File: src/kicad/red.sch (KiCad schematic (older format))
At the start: 0 parts

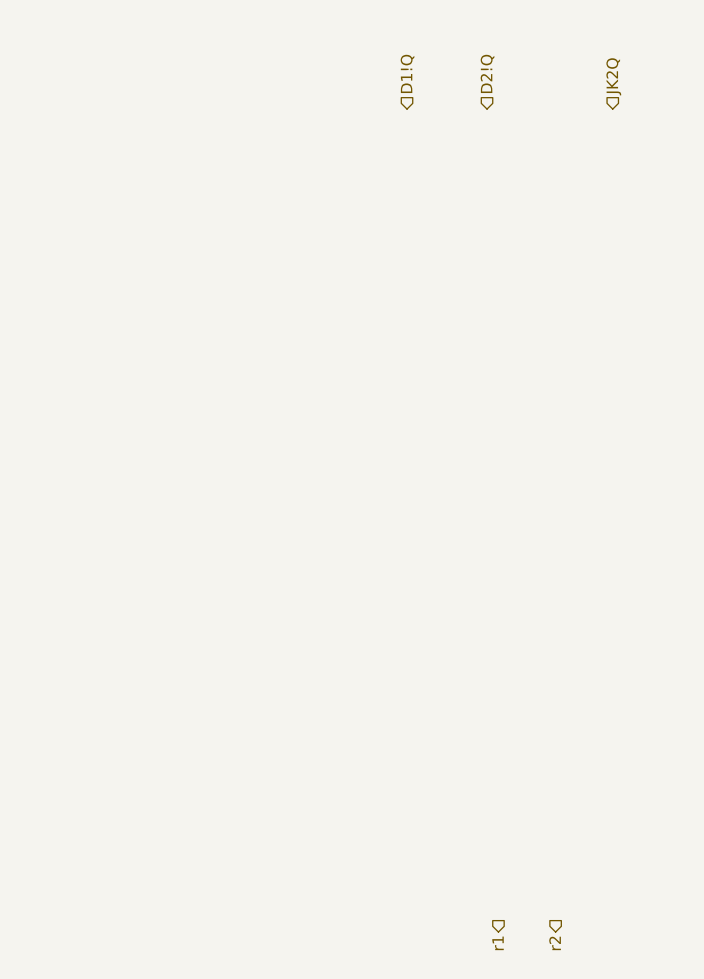
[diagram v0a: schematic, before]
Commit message: finished sub-schemes for LEDs
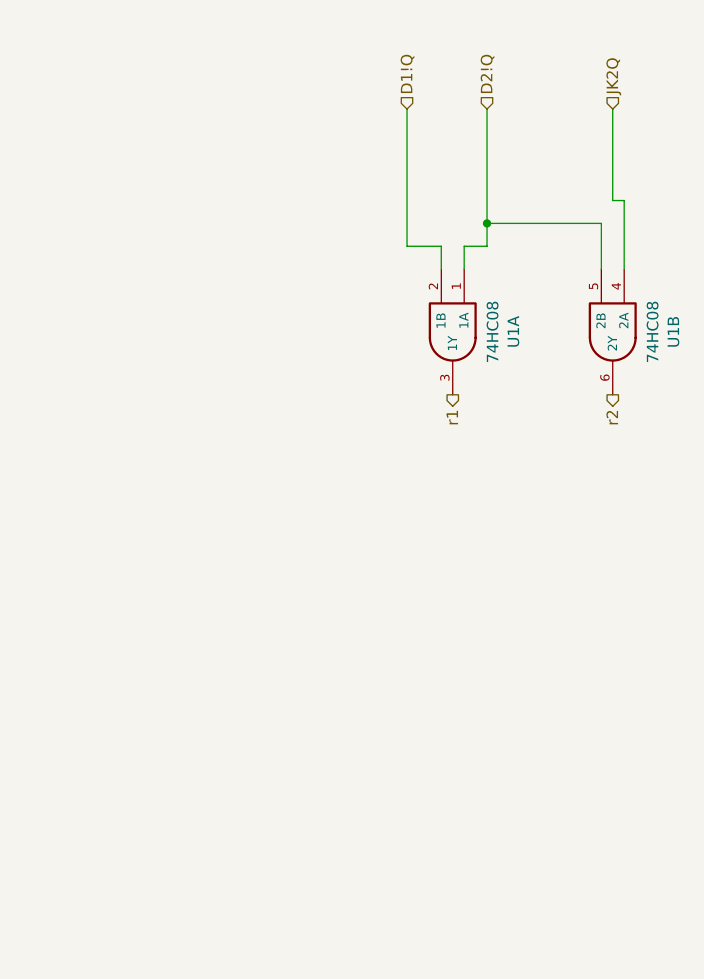
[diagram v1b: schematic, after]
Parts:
- added U1: 74HC08, Housings_SOIC:SOIC-14_3.9x8.7mm_Pitch1.27mm, symbol PB170:74HC08
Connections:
- net D1!Q: now also U1.2 (1B)
- net D2!Q: now also U1.1 (1A), U1.5 (2B)
- net JK2Q: now also U1.4 (2A)
- net r1: now also U1.3 (1Y)
- net r2: now also U1.6 (2Y)
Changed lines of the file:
@@
 Text HLabel 3650 2300 1    50   Input ~ 0
 JK2Q
-Text HLabel 3150 5850 3    50   Output ~ 0
+Text HLabel 2950 3550 3    50   Output ~ 0
 r1
-Text HLabel 3400 5850 3    50   Output ~ 0
+Text HLabel 3650 3550 3    50   Output ~ 0
 r2
+$Comp
+L PB170:74HC08 U?
+U 1 1 5FFDC9CB
+P 2950 3250
+AR Path="/5FFDC9CB" Ref="U?"  Part="2"
+AR Path="/6009AD55/5FFDC9CB" Ref="U1"  Part="1"
+F 0 "U1" H 2975 3517 50  0000 C CNN
+F 1 "74HC08" H 2975 3426 50  0000 C CNN
+F 2 "Housings_SOIC:SOIC-14_3.9x8.7mm_Pitch1.27mm" H 2950 3250 50  0001 C CNN
+F 3 "https://datasheet.lcsc.com/szlcsc/Nexperia-74HC08D-653_C5593.pdf" H 2950 3250 50  0001 C CNN
+F 4 "C5593" H 2950 3250 50  0001 C CNN "LCSC"
+	1    2950 3250
+	0    1    1    0
+$EndComp
+$Comp
+L PB170:74HC08 U?
+U 2 1 5FFDE494
+P 3650 3250
+AR Path="/5FFDE494" Ref="U?"  Part="2"
+AR Path="/6009AD55/5FFDE494" Ref="U1"  Part="2"
+F 0 "U1" H 3675 3517 50  0000 C CNN
+F 1 "74HC08" H 3675 3426 50  0000 C CNN
+F 2 "Housings_SOIC:SOIC-14_3.9x8.7mm_Pitch1.27mm" H 3650 3250 50  0001 C CNN
+F 3 "https://datasheet.lcsc.com/szlcsc/Nexperia-74HC08D-653_C5593.pdf" H 3650 3250 50  0001 C CNN
+F 4 "C5593" H 3650 3250 50  0001 C CNN "LCSC"
+	2    3650 3250
+	0    1    1    0
+$EndComp
+Wire Wire Line
+	2750 2300 2750 2900
+Wire Wire Line
+	2750 2900 2900 2900
+Wire Wire Line
+	2900 2900 2900 3000
+Wire Wire Line
+	3100 2300 3100 2800
+Wire Wire Line
+	3100 2900 3000 2900
+Wire Wire Line
+	3000 2900 3000 3000
+Wire Wire Line
+	3650 2300 3650 2700
+Wire Wire Line
+	3650 2700 3700 2700
+Wire Wire Line
+	3700 2700 3700 3000
+Wire Wire Line
+	3100 2800 3600 2800
+Wire Wire Line
+	3600 2800 3600 3000
+Connection ~ 3100 2800
+Wire Wire Line
+	3100 2800 3100 2900
 $EndSCHEMATC

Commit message: Partially fixed footprint library and reassigning references
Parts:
- U1: footprint Housings_SOIC:SOIC-14_3.9x8.7mm_Pitch1.27mm -> Housing_SOIC:SOIC-14_3.9x8.7mm_Pitch1.27mm
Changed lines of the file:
@@
 F 0 "U1" H 3675 3517 50  0000 C CNN
 F 1 "74HC08" H 3675 3426 50  0000 C CNN
-F 2 "Housings_SOIC:SOIC-14_3.9x8.7mm_Pitch1.27mm" H 3650 3250 50  0001 C CNN
+F 2 "Housing_SOIC:SOIC-14_3.9x8.7mm_Pitch1.27mm" H 3650 3250 50  0001 C CNN
 F 3 "https://datasheet.lcsc.com/szlcsc/Nexperia-74HC08D-653_C5593.pdf" H 3650 3250 50  0001 C CNN
 F 4 "C5593" H 3650 3250 50  0001 C CNN "LCSC"
@@
 F 0 "U1" H 2975 3517 50  0000 C CNN
 F 1 "74HC08" H 2975 3426 50  0000 C CNN
-F 2 "Housings_SOIC:SOIC-14_3.9x8.7mm_Pitch1.27mm" H 2950 3250 50  0001 C CNN
+F 2 "Housing_SOIC:SOIC-14_3.9x8.7mm_Pitch1.27mm" H 2950 3250 50  0001 C CNN
 F 3 "https://datasheet.lcsc.com/szlcsc/Nexperia-74HC08D-653_C5593.pdf" H 2950 3250 50  0001 C CNN
 F 4 "C5593" H 2950 3250 50  0001 C CNN "LCSC"

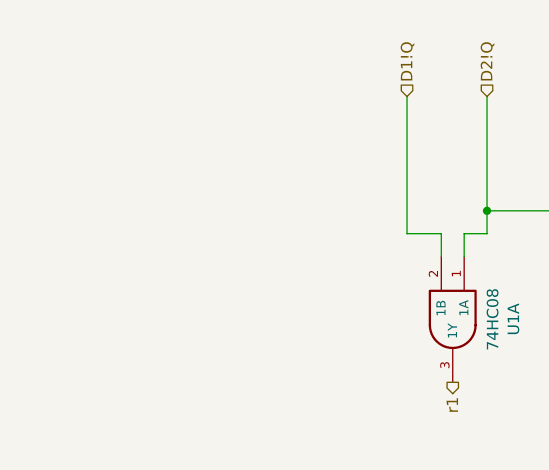
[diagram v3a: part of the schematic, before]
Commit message: added annotations, power connections to parts
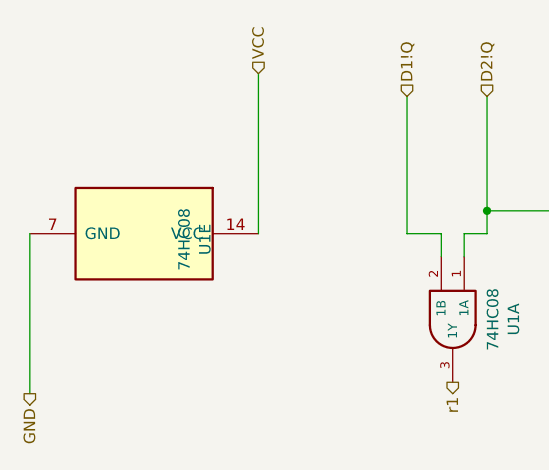
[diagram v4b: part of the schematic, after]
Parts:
- added unit 5 of U1
- U1: footprint Housing_SOIC:SOIC-14_3.9x8.7mm_Pitch1.27mm -> Package_SO:SOIC-14_3.9x8.7mm_P1.27mm
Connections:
- new net GND: U1.7 (GND)
- new net VCC: U1.14 (VCC)
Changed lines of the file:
@@
 F 0 "U1" H 3675 3517 50  0000 C CNN
 F 1 "74HC08" H 3675 3426 50  0000 C CNN
-F 2 "Housing_SOIC:SOIC-14_3.9x8.7mm_Pitch1.27mm" H 3650 3250 50  0001 C CNN
+F 2 "Package_SO:SOIC-14_3.9x8.7mm_P1.27mm" H 3650 3250 50  0001 C CNN
 F 3 "https://datasheet.lcsc.com/szlcsc/Nexperia-74HC08D-653_C5593.pdf" H 3650 3250 50  0001 C CNN
 F 4 "C5593" H 3650 3250 50  0001 C CNN "LCSC"
@@
 F 0 "U1" H 2975 3517 50  0000 C CNN
 F 1 "74HC08" H 2975 3426 50  0000 C CNN
-F 2 "Housing_SOIC:SOIC-14_3.9x8.7mm_Pitch1.27mm" H 2950 3250 50  0001 C CNN
+F 2 "Package_SO:SOIC-14_3.9x8.7mm_P1.27mm" H 2950 3250 50  0001 C CNN
 F 3 "https://datasheet.lcsc.com/szlcsc/Nexperia-74HC08D-653_C5593.pdf" H 2950 3250 50  0001 C CNN
 F 4 "C5593" H 2950 3250 50  0001 C CNN "LCSC"
@@
 	0    1    1    0
 $EndComp
+$Comp
+L PB170:74HC08 U?
+U 5 1 606E2846
+P 1600 2900
+AR Path="/606E2846" Ref="U?"  Part="2"
+AR Path="/6006FC3B/606E2846" Ref="U?"  Part="4"
+AR Path="/6004480C/606E2846" Ref="U?"  Part="5"
+AR Path="/6009AD55/606E2846" Ref="U1"  Part="5"
+F 0 "U1" H 1625 3167 50  0000 C CNN
+F 1 "74HC08" H 1625 3076 50  0000 C CNN
+F 2 "Package_SO:SOIC-14_3.9x8.7mm_P1.27mm" H 1600 2900 50  0001 C CNN
+F 3 "https://datasheet.lcsc.com/szlcsc/Nexperia-74HC08D-653_C5593.pdf" H 1600 2900 50  0001 C CNN
+F 4 "C5593" H 1600 2900 50  0001 C CNN "LCSC"
+	5    1600 2900
+	0    1    1    0
+$EndComp
+Wire Wire Line
+	2100 2900 2100 2200
+Wire Wire Line
+	1100 2900 1100 3600
+Text HLabel 2100 2200 1    50   Input ~ 0
+VCC
+Text HLabel 1100 3600 3    50   Output ~ 0
+GND
 $EndSCHEMATC

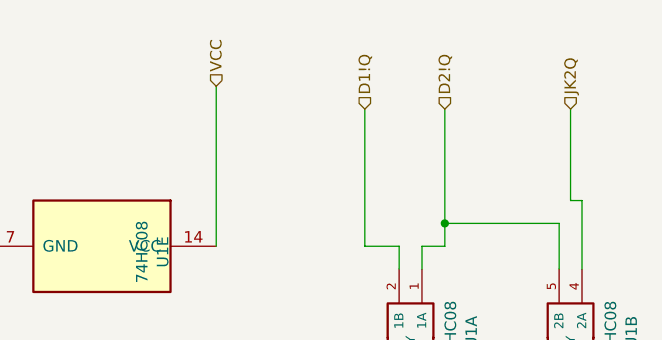
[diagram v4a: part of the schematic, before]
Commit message: Corrected negations
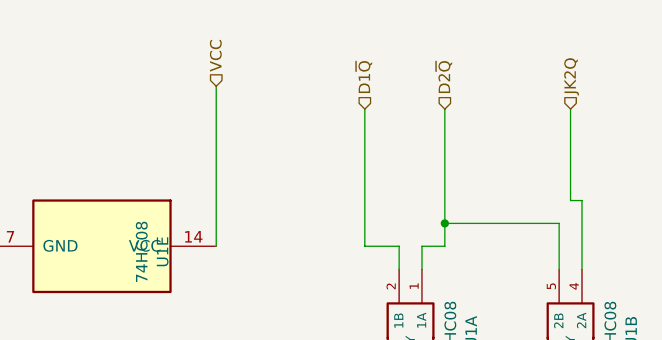
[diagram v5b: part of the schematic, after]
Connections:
- net D1!Q renamed D1~Q
- net D2!Q renamed D2~Q
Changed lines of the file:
@@
 $EndDescr
 Text HLabel 2750 2300 1    50   Input ~ 0
-D1!Q
+D1~Q
 Text HLabel 3100 2300 1    50   Input ~ 0
-D2!Q
+D2~Q
 Text HLabel 3650 2300 1    50   Input ~ 0
 JK2Q
